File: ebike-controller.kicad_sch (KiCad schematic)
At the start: 0 parts

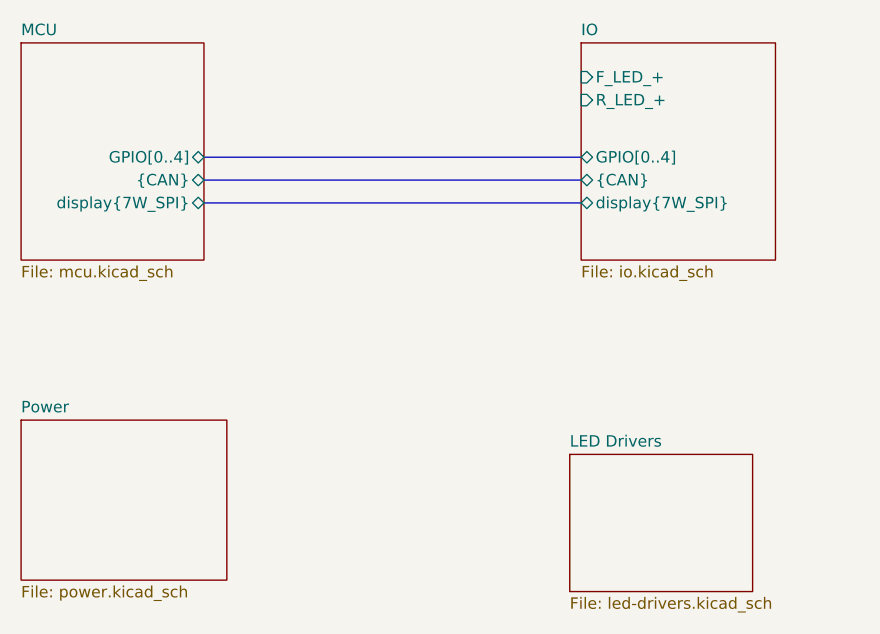
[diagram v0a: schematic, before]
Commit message: Fix schematic review findings
Power:
- Input caps were in series with VIN; now VIN->GND, VIN tied to supply
- U4 (5V) runs from protected battery rail: 60V PTC, SS210 reverse-
  polarity diode, SMBJ43A TVS, 47uF/100V bulk; EN UVLO divider (30.3V/24.2V)
- U3 (3V3) cascaded from +5V so the MCU runs on USB power too
- TPS2116 power mux: buck has priority, USB VBUS fallback, no backfeed
- Output caps redesigned per TI Table 8-1 (LM6xx25 column); L2 -> 10uH
- U3 PG drives NRST (pulled to 3V3)
- Project LM656x5 symbol: EP numbered 21, PG/RT/MODE/VCC pin types fixed,
  limit text 65V (stock KiCad symbol had all of these wrong)
- New TI_RZT0020A footprint per TI land pattern 4228518/C

MCU / IO:
- GNDA tied to GND; HSE crystal uses 2-pin symbol; load caps 33pF
- USB data connected through hierarchy; VBUS separated from +5V,
  USBLC6 ESD, VBUS sense divider on PA9
- BOOT0 10k pull-down, R2 1k, latching slide switch; switch footprints
- TCAN330 decoupling, S/SHDN tied low, termination jumper JP1
- GPIO export: 100R series + SP0505 ESD; PTCs on exported 5V/3V3
- LED resistor/colour fixes; unused MCU pins marked no-connect
- Every BOM line has manufacturer, MPN and LCSC fields
- CAN/SPI netclasses defined; power nets removed from SPI class

Co-Authored-By: Claude Opus 5.5 <noreply@anthropic.com>
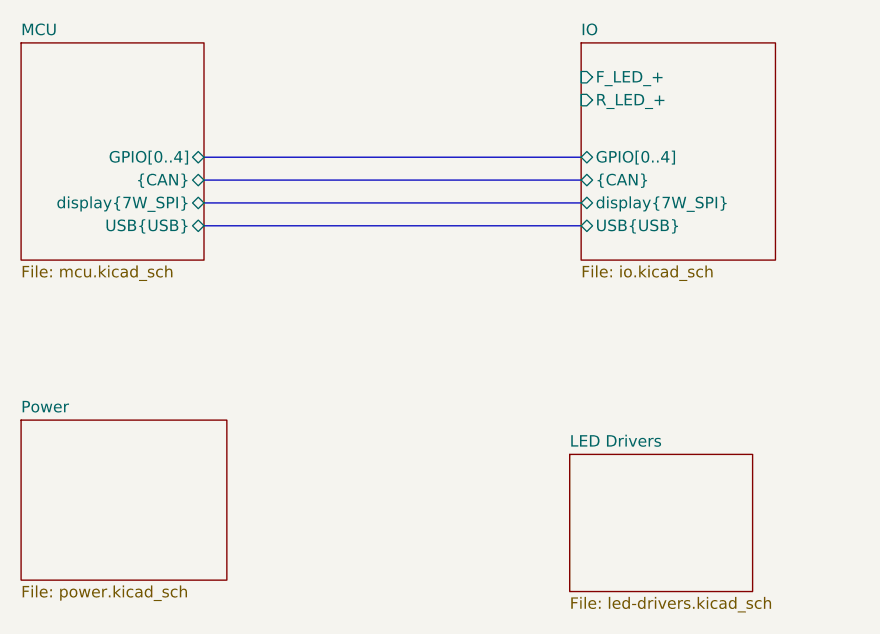
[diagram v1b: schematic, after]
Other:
- sheet IO ports: added USB{USB}; removed none
- sheet MCU ports: added USB{USB}; removed none
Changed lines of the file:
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@@
+			)
+		)
+		(pin "USB{USB}" bidirectional
+			(at 157.48 60.96 180)
+			(effects
+				(font
+					(size 1.27 1.27)
+				)
+				(justify left)
 			)
 		)
@@
 			)
 		)
+		(pin "USB{USB}" bidirectional
+			(at 115.57 60.96 0)
+			(effects
+				(font
+					(size 1.27 1.27)
+				)
+				(justify right)
+			)
+		)
 		(instances
 			(project "ebike-controller"
@@
 		)
 	)
+	(bus
+		(pts
+			(xy 115.57 60.96) (xy 157.48 60.96)
+		)
+		(stroke
+			(width 0)
+			(type default)
+		)
+	)
